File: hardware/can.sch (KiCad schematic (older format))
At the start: 13 parts

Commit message: rearranged some processor I/O pins and added LEDs
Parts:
- added D? (x2): LED, symbol LED
- added R? (x2): 1k, symbol R
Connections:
- wire segments 44 -> 53
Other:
- moved on the sheet: C?, R?, U?, X?

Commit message: cleaned up most of the error check problems
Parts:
- removed U?: MCP2551, symbol MCP2551
- added U5: MCP2551_1, symbol MCP2551_1
- gave numbers to parts that had none: 16
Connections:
- no-connect marks 0 -> 5
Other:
- moved on the sheet: C10, C11, C12, C13, C8, C9, D2, D3, R10, R11, R12, R13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

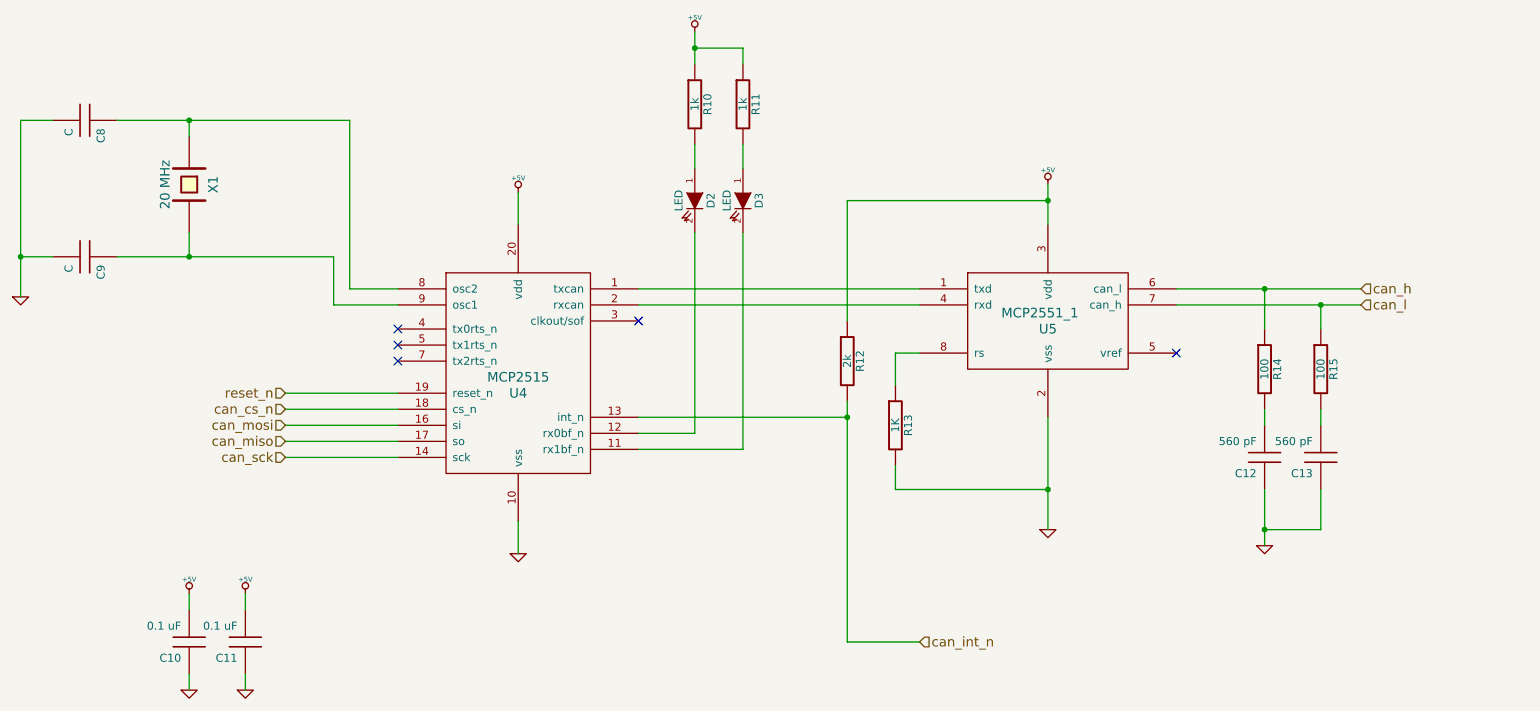
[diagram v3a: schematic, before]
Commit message: changed power supply to a lower cost TI part.  Still some DRC errors.
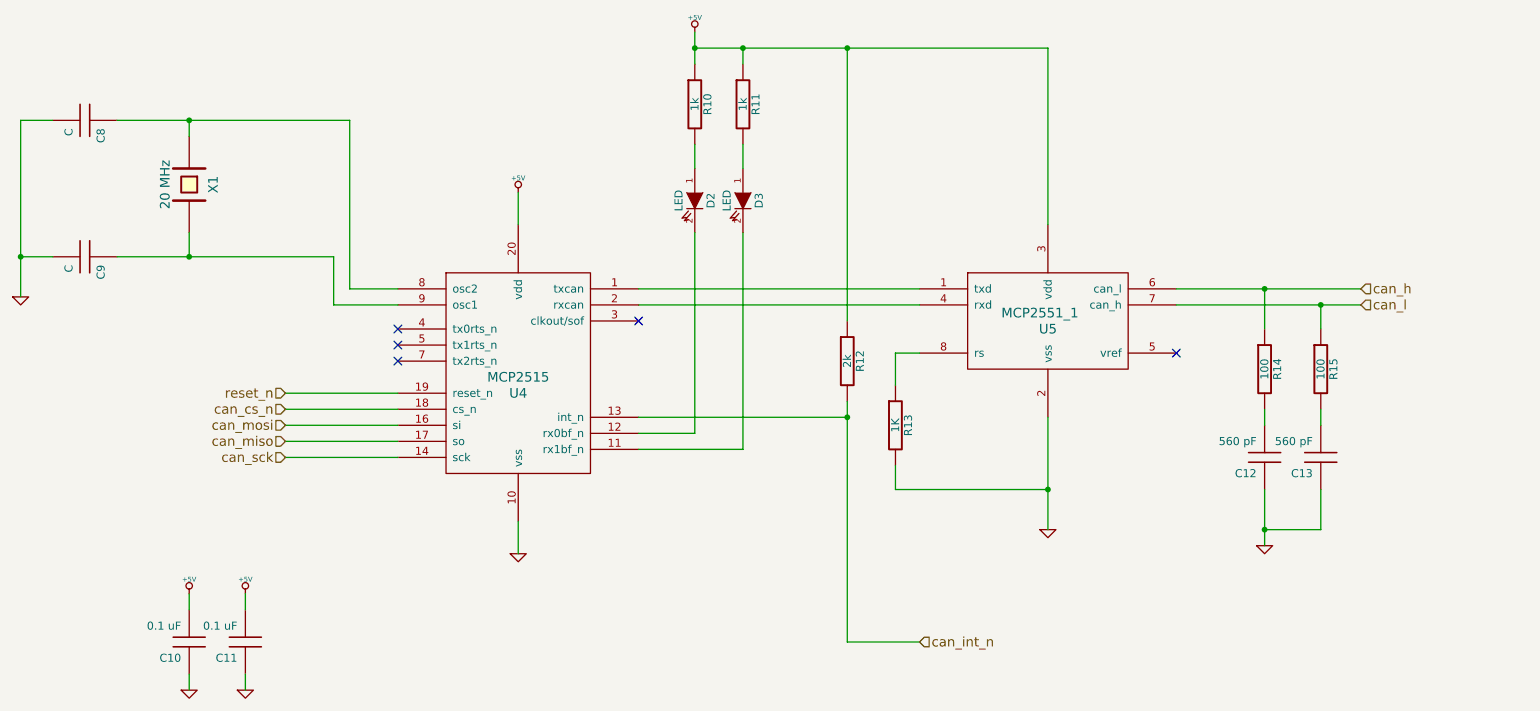
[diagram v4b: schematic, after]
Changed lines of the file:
@@
-EESchema Schematic File Version 2  date Mon 04 Nov 2013 11:57:20 AM EST
+EESchema Schematic File Version 2  date Mon 04 Nov 2013 10:20:59 PM EST
 LIBS:power
 LIBS:device
@@
 Sheet 3 5
 Title ""
-Date "4 nov 2013"
+Date "5 nov 2013"
 Rev ""
 Comp ""
@@
 $EndDescr
 Wire Wire Line
-	6500 4400 6500 4200
-Wire Wire Line
-	6500 4200 6650 4200
+	7450 3400 7450 2300
+Connection ~ 5550 2300
+Wire Wire Line
+	7450 2300 5250 2300
+Wire Wire Line
+	4900 3800 6650 3800
+Wire Wire Line
+	5550 3450 5550 4800
+Wire Wire Line
+	5550 4800 4900 4800
+Wire Wire Line
+	5550 2900 5550 3050
+Connection ~ 5250 2300
+Wire Wire Line
+	5550 2300 5550 2400
+Wire Wire Line
+	2450 5700 2450 5800
+Wire Wire Line
+	2450 6200 2450 6300
+Wire Wire Line
+	2100 6200 2100 6300
+Connection ~ 8800 5300
+Wire Wire Line
+	8800 5300 9150 5300
+Wire Wire Line
+	9150 5300 9150 5050
+Connection ~ 9150 3900
+Wire Wire Line
+	9150 3900 9150 4050
+Wire Wire Line
+	8800 4550 8800 4650
+Wire Wire Line
+	6650 6000 6200 6000
+Wire Wire Line
+	6200 4600 4900 4600
+Wire Wire Line
+	9400 3800 8250 3800
+Wire Wire Line
+	3400 4750 2700 4750
+Wire Wire Line
+	3400 4550 2700 4550
+Connection ~ 7450 5050
+Wire Wire Line
+	7450 5050 6500 5050
+Wire Wire Line
+	6500 5050 6500 4900
+Connection ~ 2100 2750
+Wire Wire Line
+	2100 2850 2100 2750
+Connection ~ 1050 3600
+Wire Wire Line
+	1250 3600 1050 3600
+Wire Wire Line
+	1050 3850 1050 2750
+Wire Wire Line
+	1050 2750 1250 2750
+Wire Wire Line
+	7450 4600 7450 5300
+Wire Wire Line
+	4150 5250 4150 5450
+Wire Wire Line
+	4150 3400 4150 3200
+Wire Wire Line
+	3400 3800 3100 3800
+Wire Wire Line
+	3100 3800 3100 2750
+Wire Wire Line
+	3100 2750 1650 2750
+Wire Wire Line
+	3400 3900 3000 3900
+Wire Wire Line
+	3000 3900 3000 3600
+Wire Wire Line
+	3000 3600 1650 3600
+Wire Wire Line
+	2100 3450 2100 3600
+Connection ~ 2100 3600
+Wire Wire Line
+	3400 4450 2700 4450
+Wire Wire Line
+	3400 4650 2700 4650
+Wire Wire Line
+	3400 4850 2700 4850
+Wire Wire Line
+	9400 3900 8250 3900
+Wire Wire Line
+	6200 6000 6200 4500
+Connection ~ 6200 4600
+Wire Wire Line
+	8800 4050 8800 3800
+Connection ~ 8800 3800
+Wire Wire Line
+	8800 5400 8800 5050
+Wire Wire Line
+	9150 4550 9150 4650
+Wire Wire Line
+	2100 5700 2100 5800
+Wire Wire Line
+	5250 2400 5250 2200
+Wire Wire Line
+	5250 2900 5250 3050
+Wire Wire Line
+	4900 4700 5250 4700
+Wire Wire Line
+	5250 4700 5250 3450
 Wire Wire Line
 	6650 3900 4900 3900
 Wire Wire Line
-	5250 3450 5250 4700
-Wire Wire Line
-	5250 4700 4900 4700
-Wire Wire Line
-	5250 2900 5250 3050
-Wire Wire Line
-	5250 2400 5250 2200
-Wire Wire Line
-	2100 5700 2100 5800
-Wire Wire Line
-	9150 4550 9150 4650
-Wire Wire Line
-	8800 5400 8800 5050
-Connection ~ 8800 3800
-Wire Wire Line
-	8800 4050 8800 3800
-Connection ~ 6200 4600
-Wire Wire Line
-	6200 4500 6200 6000
-Wire Wire Line
-	9400 3900 8250 3900
-Wire Wire Line
-	3400 4850 2700 4850
-Wire Wire Line
-	3400 4650 2700 4650
-Wire Wire Line
-	3400 4450 2700 4450
-Connection ~ 2100 3600
-Wire Wire Line
-	2100 3450 2100 3600
-Wire Wire Line
-	1650 3600 3000 3600
-Wire Wire Line
-	3000 3600 3000 3900
-Wire Wire Line
-	3000 3900 3400 3900
-Wire Wire Line
-	1650 2750 3100 2750
-Wire Wire Line
-	3100 2750 3100 3800
-Wire Wire Line
-	3100 3800 3400 3800
-Wire Wire Line
-	4150 3400 4150 3200
-Wire Wire Line
-	4150 5250 4150 5450
-Wire Wire Line
-	7450 4600 7450 5300
-Wire Wire Line
-	7450 3400 7450 3150
-Wire Wire Line
-	1250 2750 1050 2750
-Wire Wire Line
-	1050 2750 1050 3850
-Wire Wire Line
-	1250 3600 1050 3600
-Connection ~ 1050 3600
-Wire Wire Line
-	2100 2850 2100 2750
-Connection ~ 2100 2750
-Wire Wire Line
-	6500 4900 6500 5050
-Wire Wire Line
-	6500 5050 7450 5050
-Connection ~ 7450 5050
-Wire Wire Line
-	3400 4550 2700 4550
-Wire Wire Line
-	3400 4750 2700 4750
-Wire Wire Line
-	9400 3800 8250 3800
-Wire Wire Line
-	6200 4600 4900 4600
-Wire Wire Line
-	6200 6000 6650 6000
-Wire Wire Line
-	6200 4000 6200 3250
-Wire Wire Line
-	6200 3250 7450 3250
-Connection ~ 7450 3250
-Wire Wire Line
-	8800 4550 8800 4650
-Wire Wire Line
-	9150 3900 9150 4050
-Connection ~ 9150 3900
-Wire Wire Line
-	9150 5050 9150 5300
-Wire Wire Line
-	9150 5300 8800 5300
-Connection ~ 8800 5300
-Wire Wire Line
-	2100 6200 2100 6300
-Wire Wire Line
-	2450 6200 2450 6300
-Wire Wire Line
-	2450 5700 2450 5800
-Wire Wire Line
-	5550 2400 5550 2300
-Wire Wire Line
-	5550 2300 5250 2300
-Connection ~ 5250 2300
-Wire Wire Line
-	5550 2900 5550 3050
-Wire Wire Line
-	4900 4800 5550 4800
-Wire Wire Line
-	5550 4800 5550 3450
-Wire Wire Line
-	4900 3800 6650 3800
+	6650 4200 6500 4200
+Wire Wire Line
+	6500 4200 6500 4400
+Wire Wire Line
+	6200 4000 6200 2300
+Connection ~ 6200 2300
 $Comp
 L MCP2551_1 U5
@@
 NoConn ~ 3400 4050
 $Comp
-L +5V #PWR16
+L +5V #PWR010
 U 1 1 527292FD
 P 5250 2200
-F 0 "#PWR16" H 5250 2290 20  0001 C CNN
+F 0 "#PWR010" H 5250 2290 20  0001 C CNN
 F 1 "+5V" H 5250 2290 30  0000 C CNN
 	1    5250 2200
@@
 $EndComp
 $Comp
-L +5V #PWR14
+L +5V #PWR011
 U 1 1 527287C3
 P 4150 3200
-F 0 "#PWR14" H 4150 3290 20  0001 C CNN
+F 0 "#PWR011" H 4150 3290 20  0001 C CNN
 F 1 "+5V" H 4150 3290 30  0000 C CNN
 	1    4150 3200
@@
 $EndComp
 $Comp
-L +5V #PWR12
+L +5V #PWR012
 U 1 1 526D809E
 P 2450 5700
-F 0 "#PWR12" H 2450 5790 20  0001 C CNN
+F 0 "#PWR012" H 2450 5790 20  0001 C CNN
 F 1 "+5V" H 2450 5790 30  0000 C CNN
 	1    2450 5700
@@
 $EndComp
 $Comp
-L GND #PWR13
+L GND #PWR013
 U 1 1 526D809D
 P 2450 6300
-F 0 "#PWR13" H 2450 6300 30  0001 C CNN
+F 0 "#PWR013" H 2450 6300 30  0001 C CNN
 F 1 "GND" H 2450 6230 30  0001 C CNN
 	1    2450 6300
@@
 $EndComp
 $Comp
-L GND #PWR11
+L GND #PWR014
 U 1 1 526D8048
 P 2100 6300
-F 0 "#PWR11" H 2100 6300 30  0001 C CNN
+F 0 "#PWR014" H 2100 6300 30  0001 C CNN
 F 1 "GND" H 2100 6230 30  0001 C CNN
 	1    2100 6300
@@
 $EndComp
 $Comp
-L GND #PWR19
+L GND #PWR015
 U 1 1 52653C19
 P 8800 5400
-F 0 "#PWR19" H 8800 5400 30  0001 C CNN
+F 0 "#PWR015" H 8800 5400 30  0001 C CNN
 F 1 "GND" H 8800 5330 30  0001 C CNN
 	1    8800 5400
@@
 $EndComp
 $Comp
-L GND #PWR9
+L GND #PWR016
 U 1 1 52653459
 P 1050 3850
-F 0 "#PWR9" H 1050 3850 30  0001 C CNN
+F 0 "#PWR016" H 1050 3850 30  0001 C CNN
 F 1 "GND" H 1050 3780 30  0001 C CNN
 	1    1050 3850
@@
 $EndComp
 $Comp
-L +5V #PWR17
-U 1 1 52653257
-P 7450 3150
-F 0 "#PWR17" H 7450 3240 20  0001 C CNN
-F 1 "+5V" H 7450 3240 30  0000 C CNN
-	1    7450 3150
-	1    0    0    -1
-$EndComp
-$Comp
-L +5V #PWR10
+L +5V #PWR018
 U 1 1 52653250
 P 2100 5700
-F 0 "#PWR10" H 2100 5790 20  0001 C CNN
+F 0 "#PWR018" H 2100 5790 20  0001 C CNN
 F 1 "+5V" H 2100 5790 30  0000 C CNN
 	1    2100 5700
@@
 $EndComp
 $Comp
-L GND #PWR18
+L GND #PWR019
 U 1 1 52653212
 P 7450 5300
-F 0 "#PWR18" H 7450 5300 30  0001 C CNN
+F 0 "#PWR019" H 7450 5300 30  0001 C CNN
 F 1 "GND" H 7450 5230 30  0001 C CNN
 	1    7450 5300
@@
 $EndComp
 $Comp
-L GND #PWR15
+L GND #PWR020
 U 1 1 5265320A
 P 4150 5450
-F 0 "#PWR15" H 4150 5450 30  0001 C CNN
+F 0 "#PWR020" H 4150 5450 30  0001 C CNN
 F 1 "GND" H 4150 5380 30  0001 C CNN
 	1    4150 5450

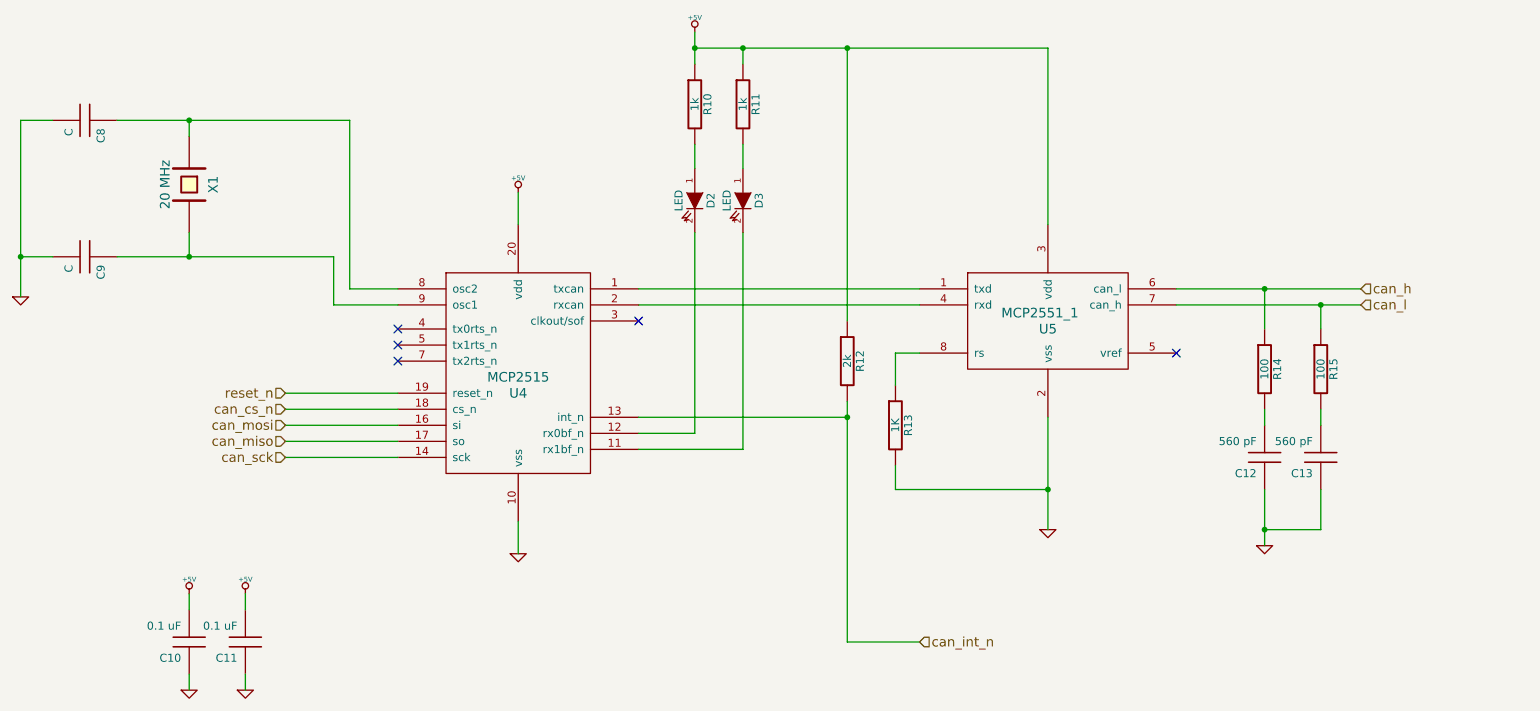
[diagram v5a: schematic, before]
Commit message: added RCT and accellerometer, added new sheet
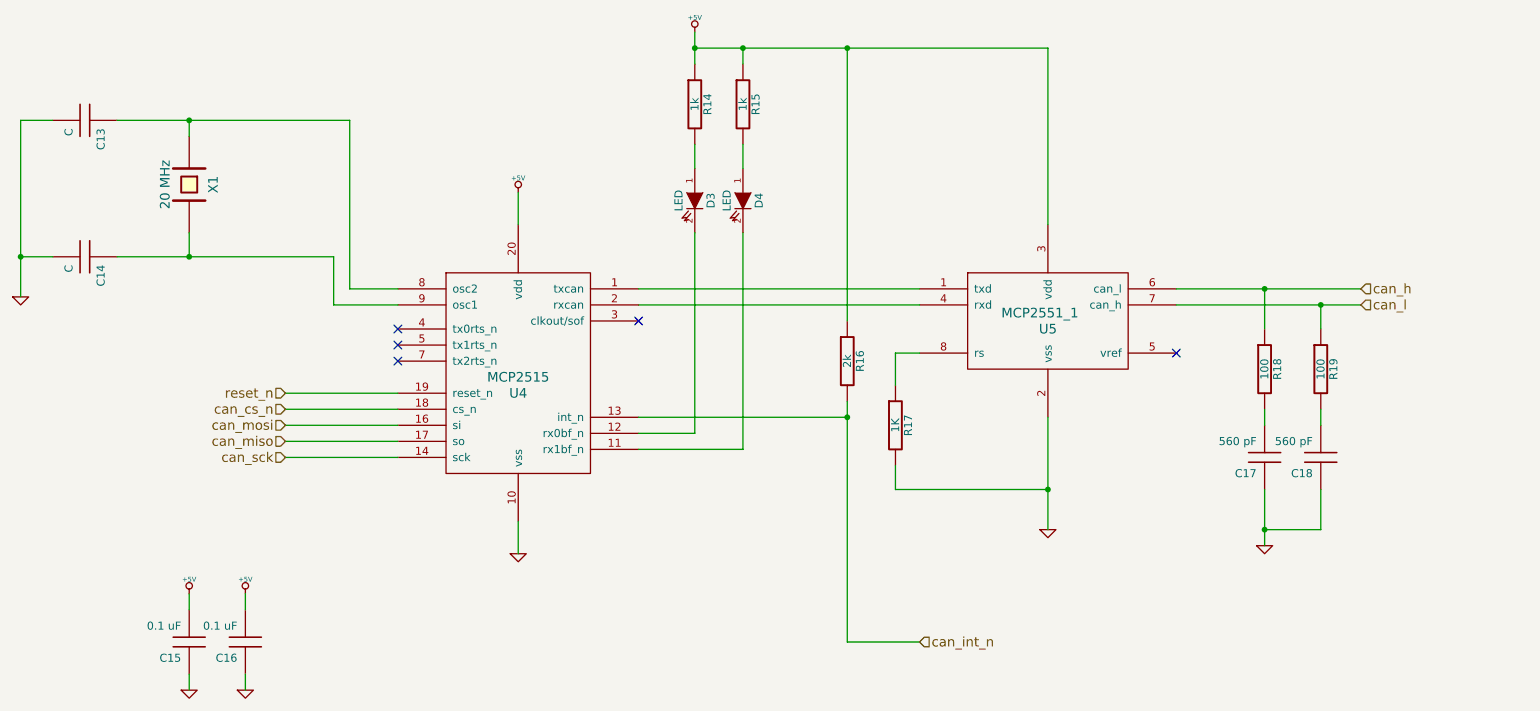
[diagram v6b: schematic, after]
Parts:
- renumbered C8 to C13, C9 to C14, C10 to C15, C11 to C16, C12 to C17, C13 to C18, D2 to D3, D3 to D4, R10 to R14, R11 to R15, R12 to R16, R13 to R17, R14 to R18, R15 to R19
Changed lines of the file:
@@
-EESchema Schematic File Version 2  date Thu 07 Nov 2013 07:55:20 AM EST
+EESchema Schematic File Version 2  date Tue 12 Nov 2013 10:09:33 PM EST
 LIBS:power
 LIBS:device
@@
 $Descr A 11000 8500
 encoding utf-8
-Sheet 3 5
+Sheet 3 6
 Title ""
-Date "7 nov 2013"
+Date "13 nov 2013"
 Rev ""
 Comp ""
@@
 NoConn ~ 3400 4050
 $Comp
-L +5V #PWR010
+L +5V #PWR012
 U 1 1 527292FD
 P 5250 2200
-F 0 "#PWR010" H 5250 2290 20  0001 C CNN
+F 0 "#PWR012" H 5250 2290 20  0001 C CNN
 F 1 "+5V" H 5250 2290 30  0000 C CNN
 	1    5250 2200
@@
 $EndComp
 $Comp
-L R R11
+L R R15
 U 1 1 527292F3
 P 5550 2650
-F 0 "R11" V 5630 2650 50  0000 C CNN
+F 0 "R15" V 5630 2650 50  0000 C CNN
 F 1 "1k" V 5550 2650 50  0000 C CNN
 	1    5550 2650
@@
 $EndComp
 $Comp
-L R R10
+L R R14
 U 1 1 527292E1
 P 5250 2650
-F 0 "R10" V 5330 2650 50  0000 C CNN
+F 0 "R14" V 5330 2650 50  0000 C CNN
 F 1 "1k" V 5250 2650 50  0000 C CNN
 	1    5250 2650
@@
 $EndComp
 $Comp
-L LED D3
+L LED D4
 U 1 1 527292D6
 P 5550 3250
-F 0 "D3" H 5550 3350 50  0000 C CNN
+F 0 "D4" H 5550 3350 50  0000 C CNN
 F 1 "LED" H 5550 3150 50  0000 C CNN
 	1    5550 3250
@@
 $EndComp
 $Comp
-L LED D2
+L LED D3
 U 1 1 527292B1
 P 5250 3250
-F 0 "D2" H 5250 3350 50  0000 C CNN
+F 0 "D3" H 5250 3350 50  0000 C CNN
 F 1 "LED" H 5250 3150 50  0000 C CNN
 	1    5250 3250
@@
 $EndComp
 $Comp
-L +5V #PWR011
+L +5V #PWR013
 U 1 1 527287C3
 P 4150 3200
-F 0 "#PWR011" H 4150 3290 20  0001 C CNN
+F 0 "#PWR013" H 4150 3290 20  0001 C CNN
 F 1 "+5V" H 4150 3290 30  0000 C CNN
 	1    4150 3200
@@
 $EndComp
 $Comp
-L +5V #PWR012
+L +5V #PWR014
 U 1 1 526D809E
 P 2450 5700
-F 0 "#PWR012" H 2450 5790 20  0001 C CNN
+F 0 "#PWR014" H 2450 5790 20  0001 C CNN
 F 1 "+5V" H 2450 5790 30  0000 C CNN
 	1    2450 5700
@@
 $EndComp
 $Comp
-L GND #PWR013
+L GND #PWR015
 U 1 1 526D809D
 P 2450 6300
-F 0 "#PWR013" H 2450 6300 30  0001 C CNN
+F 0 "#PWR015" H 2450 6300 30  0001 C CNN
 F 1 "GND" H 2450 6230 30  0001 C CNN
 	1    2450 6300
@@
 $EndComp
 $Comp
-L C C11
+L C C16
 U 1 1 526D809C
 P 2450 6000
-F 0 "C11" H 2500 6100 50  0000 L CNN
+F 0 "C16" H 2500 6100 50  0000 L CNN
 F 1 "0.1 uF" H 2500 5900 50  0000 L CNN
 	1    2450 6000
@@
 $EndComp
 $Comp
-L C C10
+L C C15
 U 1 1 526D8053
 P 2100 6000
-F 0 "C10" H 2150 6100 50  0000 L CNN
+F 0 "C15" H 2150 6100 50  0000 L CNN
 F 1 "0.1 uF" H 2150 5900 50  0000 L CNN
 	1    2100 6000
@@
 $EndComp
 $Comp
-L GND #PWR014
+L GND #PWR016
 U 1 1 526D8048
 P 2100 6300
-F 0 "#PWR014" H 2100 6300 30  0001 C CNN
+F 0 "#PWR016" H 2100 6300 30  0001 C CNN
 F 1 "GND" H 2100 6230 30  0001 C CNN
 	1    2100 6300
@@
 $EndComp
 $Comp
-L GND #PWR015
+L GND #PWR017
 U 1 1 52653C19
 P 8800 5400
-F 0 "#PWR015" H 8800 5400 30  0001 C CNN
+F 0 "#PWR017" H 8800 5400 30  0001 C CNN
 F 1 "GND" H 8800 5330 30  0001 C CNN
 	1    8800 5400
@@
 $EndComp
 $Comp
-L C C13
+L C C18
 U 1 1 52653BFD
 P 9150 4850
-F 0 "C13" H 9200 4950 50  0000 L CNN
+F 0 "C18" H 9200 4950 50  0000 L CNN
 F 1 "560 pF" H 9200 4750 50  0000 L CNN
 	1    9150 4850
@@
 $EndComp
 $Comp
-L C C12
+L C C17
 U 1 1 52653BE2
 P 8800 4850
-F 0 "C12" H 8850 4950 50  0000 L CNN
+F 0 "C17" H 8850 4950 50  0000 L CNN
 F 1 "560 pF" H 8850 4750 50  0000 L CNN
 	1    8800 4850
@@
 $EndComp
 $Comp
-L R R15
+L R R19
 U 1 1 52653BCF
 P 9150 4300
-F 0 "R15" V 9230 4300 50  0000 C CNN
+F 0 "R19" V 9230 4300 50  0000 C CNN
 F 1 "100" V 9150 4300 50  0000 C CNN
 	1    9150 4300
@@
 $EndComp
 $Comp
-L R R14
+L R R18
 U 1 1 52653BC8
 P 8800 4300
-F 0 "R14" V 8880 4300 50  0000 C CNN
+F 0 "R18" V 8880 4300 50  0000 C CNN
 F 1 "100" V 8800 4300 50  0000 C CNN
 	1    8800 4300
@@
 $EndComp
 $Comp
-L R R12
+L R R16
 U 1 1 5265384F
 P 6200 4250
-F 0 "R12" V 6280 4250 50  0000 C CNN
+F 0 "R16" V 6280 4250 50  0000 C CNN
 F 1 "2k" V 6200 4250 50  0000 C CNN
 	1    6200 4250
@@
 can_h
 $Comp
-L R R13
+L R R17
 U 1 1 526534F5
 P 6500 4650
-F 0 "R13" V 6580 4650 50  0000 C CNN
+F 0 "R17" V 6580 4650 50  0000 C CNN
 F 1 "1K" V 6500 4650 50  0000 C CNN
 	1    6500 4650
@@
 $EndComp
 $Comp
-L GND #PWR016
+L GND #PWR018
 U 1 1 52653459
 P 1050 3850
-F 0 "#PWR016" H 1050 3850 30  0001 C CNN
+F 0 "#PWR018" H 1050 3850 30  0001 C CNN
 F 1 "GND" H 1050 3780 30  0001 C CNN
 	1    1050 3850
@@
 $EndComp
 $Comp
-L C C8
+L C C13
 U 1 1 52653347
 P 1450 2750
-F 0 "C8" H 1500 2850 50  0000 L CNN
+F 0 "C13" H 1500 2850 50  0000 L CNN
 F 1 "C" H 1500 2650 50  0000 L CNN
 	1    1450 2750
@@
 $EndComp
 $Comp
-L C C9
+L C C14
 U 1 1 52653340
 P 1450 3600
-F 0 "C9" H 1500 3700 50  0000 L CNN
+F 0 "C14" H 1500 3700 50  0000 L CNN
 F 1 "C" H 1500 3500 50  0000 L CNN
 	1    1450 3600
@@
 $EndComp
 $Comp
-L +5V #PWR018
+L +5V #PWR019
 U 1 1 52653250
 P 2100 5700
-F 0 "#PWR018" H 2100 5790 20  0001 C CNN
+F 0 "#PWR019" H 2100 5790 20  0001 C CNN
 F 1 "+5V" H 2100 5790 30  0000 C CNN
 	1    2100 5700
@@
 $EndComp
 $Comp
-L GND #PWR019
+L GND #PWR020
 U 1 1 52653212
 P 7450 5300
-F 0 "#PWR019" H 7450 5300 30  0001 C CNN
+F 0 "#PWR020" H 7450 5300 30  0001 C CNN
 F 1 "GND" H 7450 5230 30  0001 C CNN
 	1    7450 5300
@@
 $EndComp
 $Comp
-L GND #PWR020
+L GND #PWR021
 U 1 1 5265320A
 P 4150 5450
-F 0 "#PWR020" H 4150 5450 30  0001 C CNN
+F 0 "#PWR021" H 4150 5450 30  0001 C CNN
 F 1 "GND" H 4150 5380 30  0001 C CNN
 	1    4150 5450
